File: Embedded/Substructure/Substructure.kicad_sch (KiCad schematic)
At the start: 13 parts, among them J1 USB, U1 Comms Link Expansion, U2 TCA9535RTWR, U3 TOF 0, U4 TOF 1, U5 FFC [U], U6 Display, U7 Expansion

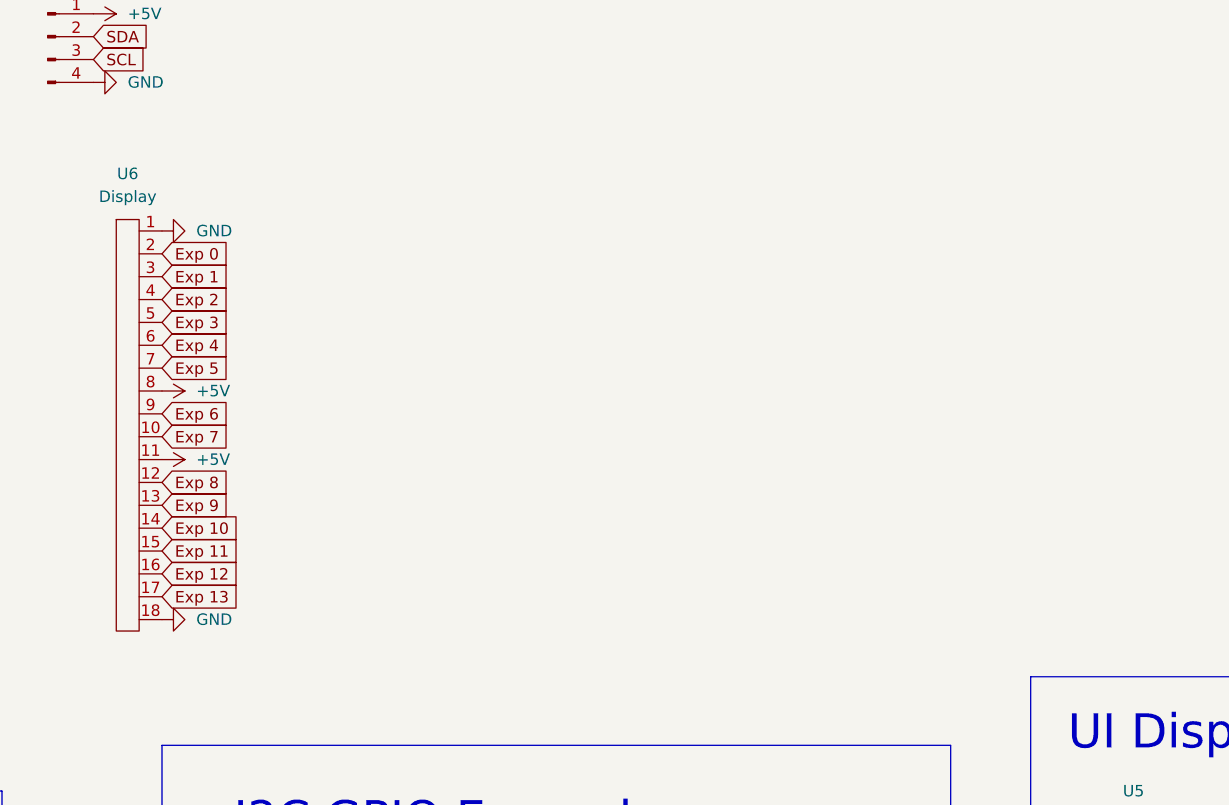
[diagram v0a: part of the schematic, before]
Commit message: Routed Most of the Pins
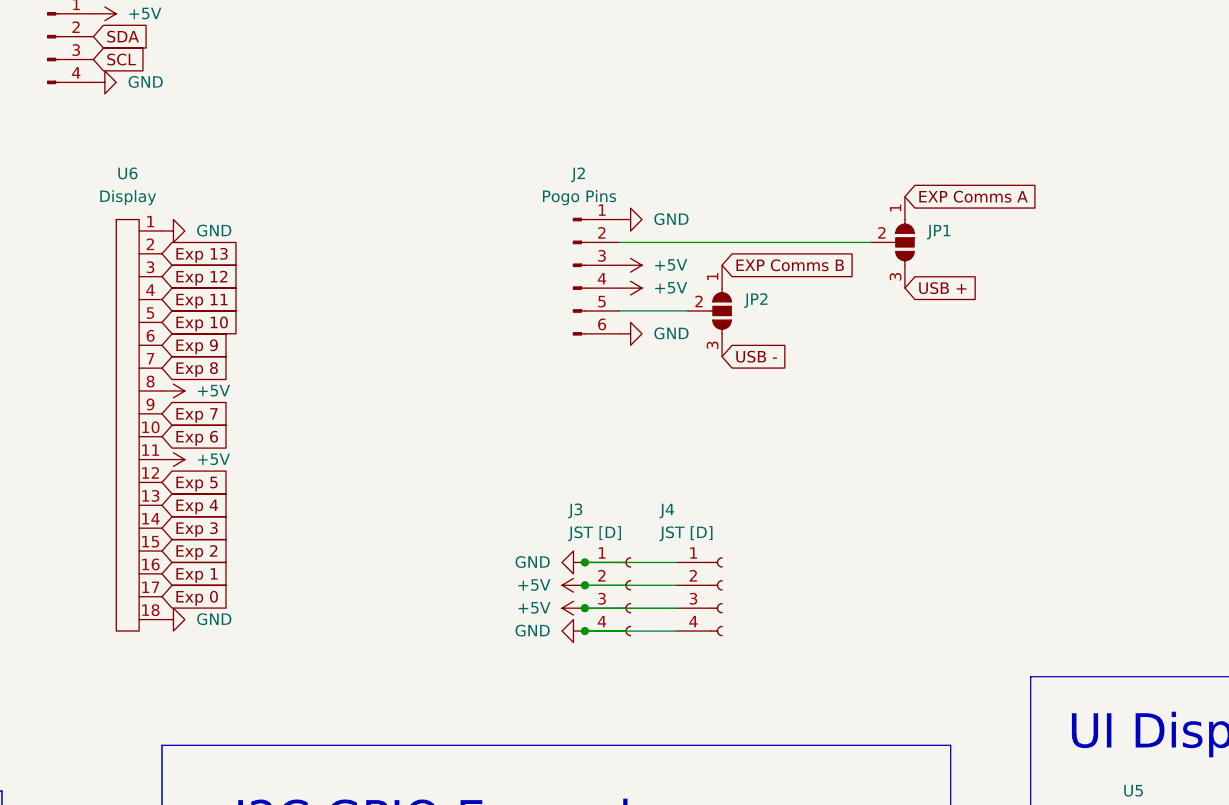
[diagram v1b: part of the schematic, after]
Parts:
- added J2: Pogo Pins, Connector_PinHeader_2.54mm:PinHeader_1x06_P2.54mm_Vertical, symbol Connector:Conn_01x06_Pin
- added J3, J4: JST [D], Connector_Molex:Molex_PicoBlade_53048-0410_1x04_P1.25mm_Horizontal, symbol Connector:Conn_01x04_Socket
- added JP1, JP2: SolderJumper_3_Open, Jumper:SolderJumper-3_P1.3mm_Open_RoundedPad1.0x1.5mm, symbol Jumper:SolderJumper_3_Open
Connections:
- net +5V: now also J2.3 (Pin_3), J2.4 (Pin_4), J3.2 (Pin_2), J3.3 (Pin_3), J4.2 (Pin_2), J4.3 (Pin_3)
- net EXP Comms A: now also JP1.1 (A)
- net EXP Comms B: now also JP2.1 (A)
- net Exp 0: now also U6.17; no longer U6.2
- net Exp 1: now also U6.16; no longer U6.3
- net Exp 10: now also U6.5; no longer U6.14
- net Exp 11: now also U6.4; no longer U6.15
- net Exp 12: now also U6.3; no longer U6.16
- net Exp 13: now also U6.2; no longer U6.17
- net Exp 2: now also U6.15; no longer U6.4
- net Exp 3: now also U6.14; no longer U6.5
- net Exp 4: now also U6.13; no longer U6.6
- net Exp 5: now also U6.12; no longer U6.7
- net Exp 6: now also U6.10; no longer U6.9
- net Exp 7: now also U6.9; no longer U6.10
- net Exp 8: now also U6.7; no longer U6.12
- net Exp 9: now also U6.6; no longer U6.13
- net GND: now also J2.1 (Pin_1), J2.6 (Pin_6), J3.1 (Pin_1), J3.4 (Pin_4), J4.1 (Pin_1), J4.4 (Pin_4)
- net USB +: now also JP1.3 (B)
- net USB -: now also JP2.3 (B)
- new net: J2.2 (Pin_2), JP1.2 (C)
- new net: J2.5 (Pin_5), JP2.2 (C)

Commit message: Added Photoresistors
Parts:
- added C3, C4: 1uF, Resistor_SMD:R_0603_1608Metric, symbol Device:C
- added C5: 10uF, Capacitor_SMD:C_0603_1608Metric, symbol Device:C
- added R4, R5: R_Photo, Photoresistor:Photoresistor Aliexpress, symbol Device:R_Photo
- added R6, R7: 10K, Resistor_SMD:R_0603_1608Metric_Pad0.98x0.95mm_HandSolder, symbol Device:R
- added U8: AP7366-33W5-7, AP7366-SOT25:AP7366, symbol AP7366_SOT_25:AP7366_SOT25
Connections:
- net +3V3: now also C4.1, C5.1, R6.1, R7.1, U8.5 (Vout)
- net +5V: now also C3.1, U8.1 (VCC), U8.3 (EN)
- net EXP Comms A: now also R4.1, R6.2
- net EXP Comms B: now also R5.1, R7.2
- net GND: now also C3.2, C4.2, C5.2, R4.2, R5.2, U8.2 (GND)
- no-connect marks 0 -> 1
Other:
- moved on the sheet: J2, JP1, JP2

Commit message: Added 2nd Display Port
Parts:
- added U9: Display, FFC_Connector:FFC Aliexpress 0.5mm 18P, symbol FCC_Connector:FFC_18P
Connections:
- net +5V: now also U9.11, U9.8
- net EXP Comms A: now also JP1.3 (B); no longer JP1.1 (A)
- net EXP Comms B: now also JP2.3 (B); no longer JP2.1 (A)
- net Exp 0: now also U9.17
- net Exp 1: now also U9.16
- net Exp 10: now also U9.5
- net Exp 11: now also U9.4
- net Exp 12: now also U9.3
- net Exp 13: now also U9.2
- net Exp 2: now also U9.15
- net Exp 3: now also U9.14
- net Exp 4: now also U9.13
- net Exp 5: now also U9.12
- net Exp 6: now also U9.10
- net Exp 7: now also U9.9
- net Exp 8: now also U9.7
- net Exp 9: now also U9.6
- net GND: now also U9.1, U9.18
- net USB +: now also JP1.1 (A); no longer JP1.3 (B)
- net USB -: now also JP2.1 (A); no longer JP2.3 (B)
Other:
- moved on the sheet: U6
